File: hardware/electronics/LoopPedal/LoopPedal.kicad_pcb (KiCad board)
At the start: 2 copper layers, 1 part

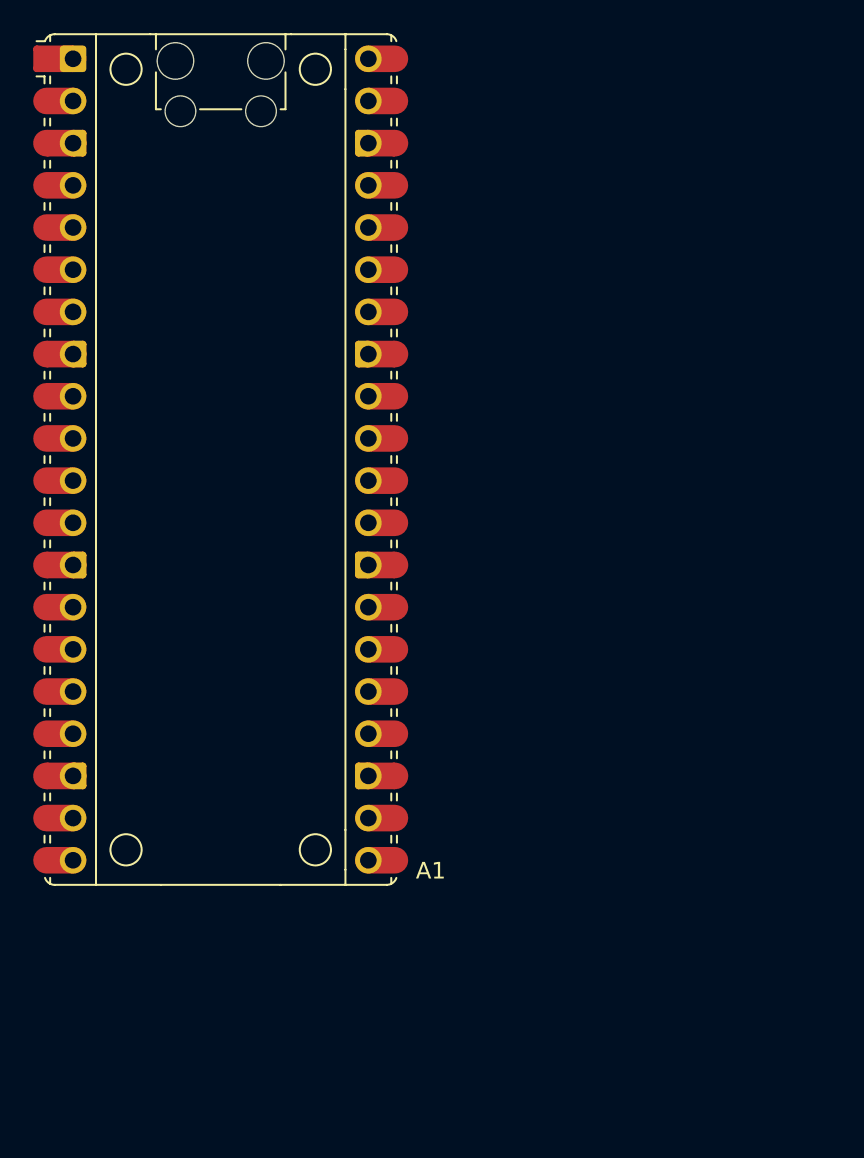
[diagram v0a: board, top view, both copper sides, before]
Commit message: adds pi pico and connectors
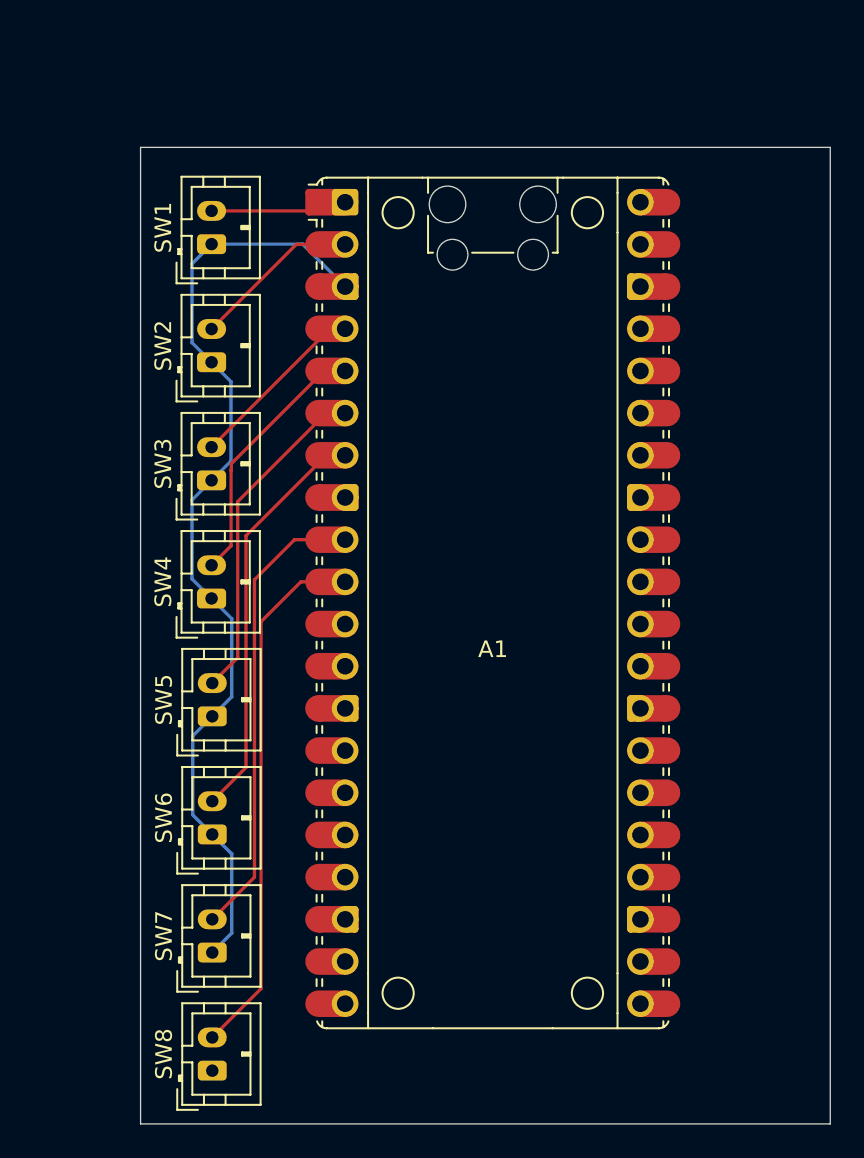
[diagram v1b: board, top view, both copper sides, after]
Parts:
- added SW1: SW_SPST, Connector_JST:JST_PH_B2B-PH-K_1x02_P2.00mm_Vertical, F.Cu at (115.5, 62.7)
- added SW2: SW_SPST, Connector_JST:JST_PH_B2B-PH-K_1x02_P2.00mm_Vertical, F.Cu at (115.5, 69.8)
- added SW3: SW_SPST, Connector_JST:JST_PH_B2B-PH-K_1x02_P2.00mm_Vertical, F.Cu at (115.5, 76.9)
- added SW4: SW_SPST, Connector_JST:JST_PH_B2B-PH-K_1x02_P2.00mm_Vertical, F.Cu at (115.5, 84.1)
- added SW5: SW_SPST, Connector_JST:JST_PH_B2B-PH-K_1x02_P2.00mm_Vertical, F.Cu at (115.6, 91.2)
- added SW6: SW_SPST, Connector_JST:JST_PH_B2B-PH-K_1x02_P2.00mm_Vertical, F.Cu at (115.6, 98.3)
- added SW7: SW_SPST, Connector_JST:JST_PH_B2B-PH-K_1x02_P2.00mm_Vertical, F.Cu at (115.6, 105.4)
- added SW8: SW_SPST, Connector_JST:JST_PH_B2B-PH-K_1x02_P2.00mm_Vertical, F.Cu at (115.6, 112.5)
- moved A1 18.5 mm to (132.5, 84.3)
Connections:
- net Net-(A1-GND-Pad13) renamed GND
- A1 pad 1: unconnected-(A1-GPIO0-Pad1) -> SW1
- A1 pad 10: unconnected-(A1-GPIO7-Pad10) -> SW8
- A1 pad 2: unconnected-(A1-GPIO1-Pad2) -> SW2
- A1 pad 4: unconnected-(A1-GPIO2-Pad4) -> SW3
- A1 pad 5: unconnected-(A1-GPIO3-Pad5) -> SW4
- A1 pad 6: unconnected-(A1-GPIO4-Pad6) -> SW5
- A1 pad 7: unconnected-(A1-GPIO5-Pad7) -> SW6
- A1 pad 9: unconnected-(A1-GPIO6-Pad9) -> SW7
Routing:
- net GND: track 0.00 -> 57.6 mm
- net SW8: track 0.00 -> 32.3 mm
- net SW7: track 0.00 -> 28.0 mm
- net SW6: track 0.00 -> 24.8 mm
- net SW5: track 0.00 -> 20.2 mm
- net SW4: track 0.00 -> 15.8 mm
- net SW3: track 0.00 -> 11.0 mm
- net SW2: track 0.00 -> 10.2 mm
- net SW1: track 0.00 -> 8.26 mm
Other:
- board outline added: 41.5 x 58.8 mm
